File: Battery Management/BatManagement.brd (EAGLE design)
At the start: 87.1 x 71.1 mm, 19 parts, among them J1 RASPBERRYPI-40-PIN-GPIO_PTH, SW1 100SP1T2B4M6QE, X1 87758-1416, X2 87758-1416, X3 22-23-2031, X4 22-23-2031

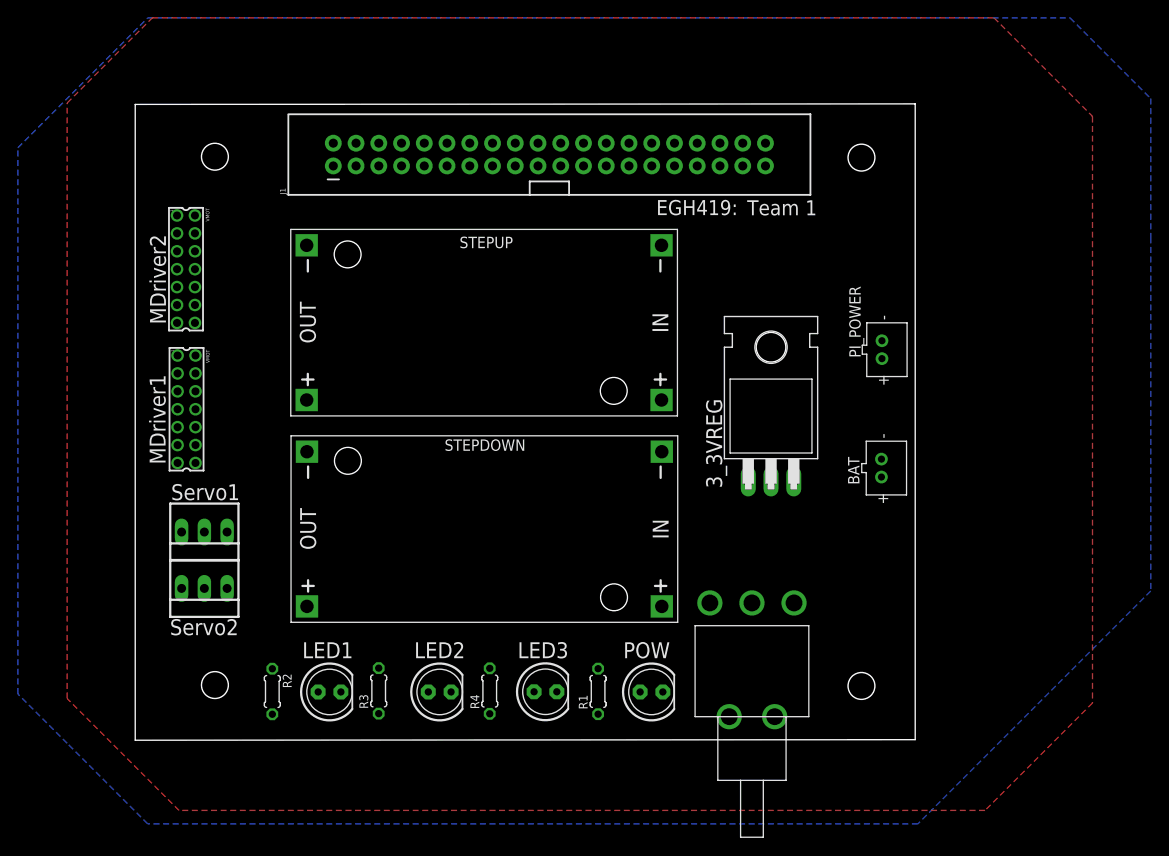
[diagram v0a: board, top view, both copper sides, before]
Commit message: Added jumper for 6V motors
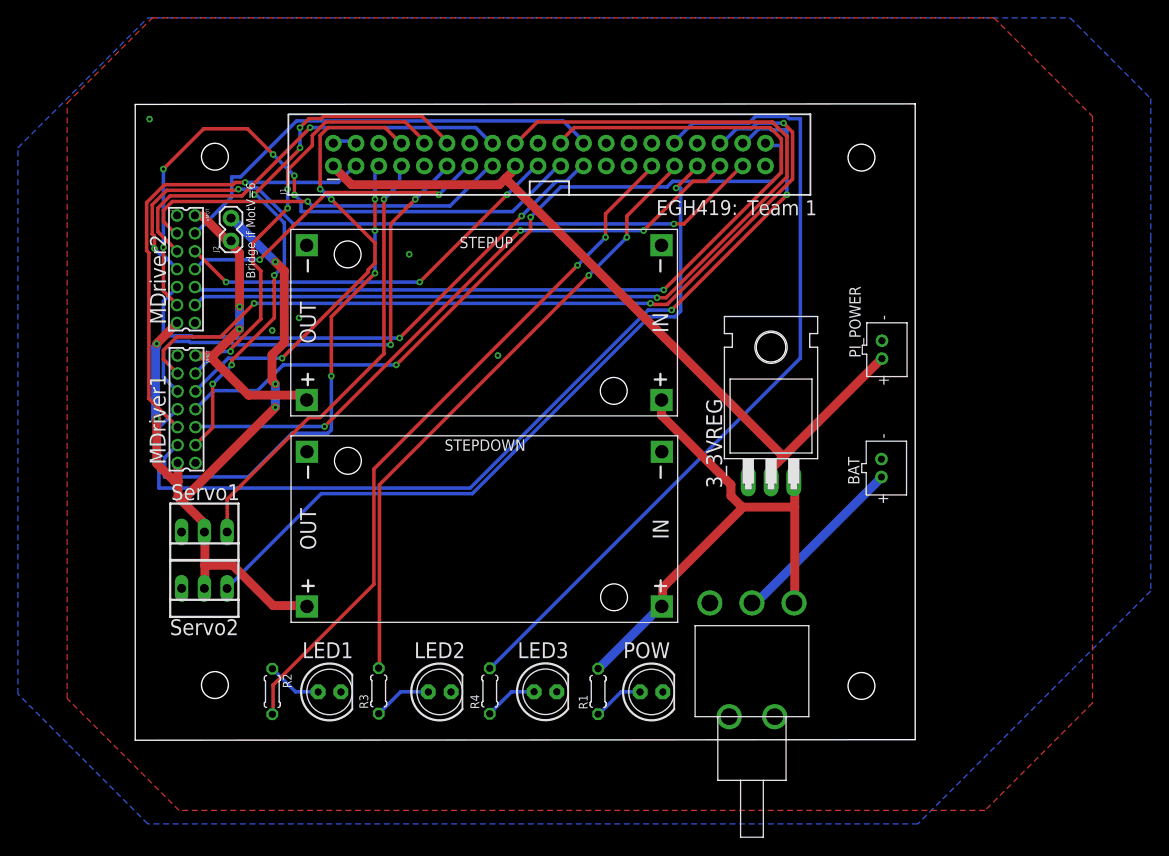
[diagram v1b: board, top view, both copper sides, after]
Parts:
- added J2: (no value), SparkFun-Connectors:1X02
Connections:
- net 5V: now also J2.2
- net ENC1A_1: now also J1.3
- net ENC1A_2: now also J1.23
- net ENC1B_1: now also J1.5
- net ENC1B_2: now also J1.21
- net ENC2A_1: now also J1.8
- net ENC2A_2: now also J1.19
- net ENC2B_1: now also J1.10
- net ENC2B_2: now also J1.24
- net IN3_1: no longer X2.12
- net IN3_2: now also X2.12
- net VMOT: now also J2.1
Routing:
- net IN3_2: track 0.00 -> 108.6 mm, vias 0 -> 1
- net ENA_1: track 0.00 -> 106.3 mm, vias 0 -> 2
- net IN4_2: track 0.00 -> 100.9 mm, vias 0 -> 1
- net IN1_1: track 0.00 -> 96.2 mm, vias 0 -> 3
- net LED3: track 0.00 -> 91.3 mm
- net 5V: track 0.00 -> 87.7 mm, vias 0 -> 5
- net 3_3V: track 0.00 -> 85.2 mm
- net ENB_1: track 0.00 -> 82.1 mm, vias 0 -> 2
- net SERVO2: track 0.00 -> 81.2 mm, vias 0 -> 1
- net ENA_2: track 0.00 -> 79.5 mm, vias 0 -> 3
- net LED1: track 0.00 -> 78.9 mm, vias 0 -> 2
- net IN4_1: track 0.00 -> 70.9 mm, vias 0 -> 3
- net ENC1B_2: track 0.00 -> 69.9 mm, vias 0 -> 5
- net LED2: track 0.00 -> 69.7 mm, vias 0 -> 2
- net IN3_1: track 0.00 -> 61.6 mm, vias 0 -> 6
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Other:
- board text added: "Bridge if MotV=6"

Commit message: Changed to standard header for mdriver connection
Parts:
- removed X1, X2: 87758-1416, con-molex:87758-1416
- added SV1, SV2: (no value), con-lsta:FE07-2
- moved J2 12.8 mm to (23.4, 95.1), turned to 270 degrees
- moved X4 4.85 mm to (26.2, 47.5), turned to 270 degrees
- moved X3 3.28 mm to (30.6, 47.5), turned to 270 degrees
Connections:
- net 5V: now also SV1.1, SV2.1; no longer X1.13, X2.13
- net ENA_1: now also SV1.7; no longer X1.7
- net ENA_2: now also SV2.7; no longer X2.7
- net ENB_1: now also SV1.8; no longer X1.8
- net ENB_2: now also SV2.8; no longer X2.8
- net ENC1A_1: now also SV1.5; no longer X1.9
- net ENC1A_2: now also SV2.5; no longer X2.9
- net ENC1B_1: now also SV1.3; no longer X1.11
- net ENC1B_2: now also SV2.3; no longer X2.11
- net ENC2A_1: now also SV1.10; no longer X1.6
- net ENC2A_2: now also SV2.10; no longer X2.6
- net ENC2B_1: now also SV1.12; no longer X1.4
- net ENC2B_2: now also SV2.12; no longer X2.4
- net GND: now also SV1.13, SV1.2, SV2.13, SV2.2; no longer X1.1, X1.14, X2.1, X2.14
- net IN1_1: now also SV1.11; no longer X1.3
- net IN1_2: now also SV2.11; no longer X2.3
- net IN2_1: now also SV1.9; no longer X1.5
- net IN2_2: now also SV2.9; no longer X2.5
- net IN3_1: now also SV1.4; no longer X1.12
- net IN3_2: now also SV2.4; no longer X2.12
- net IN4_1: now also SV1.6; no longer X1.10
- net IN4_2: now also SV2.6; no longer X2.10
- net VMOT: now also SV1.14, SV2.14; no longer X1.2, X2.2
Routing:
- net ENC2B_2: track 51.1 -> 113.8 mm, vias 0 -> 3
- net IN3_2: track 108.6 -> 54.1 mm
- net IN4_2: track 100.9 -> 57.4 mm, vias 1 -> 0
- net IN3_1: track 61.6 -> 89.1 mm, vias 6 -> 3
- net 5V: track 87.7 -> 65.6 mm, vias 5 -> 0
- net ENC1B_2: track 69.9 -> 51.7 mm, vias 5 -> 4
- net ENA_1: track 106.3 -> 91.9 mm
- net IN4_1: track 70.9 -> 81.2 mm, vias 3 -> 2
- net ENC1B_1: track 56.8 -> 47.1 mm, vias 4 -> 3
- net SERVO2: track 81.2 -> 72.0 mm
- net ENC1A_2: track 61.1 -> 53.0 mm, vias 2 -> 4
- net VMOT: track 34.4 -> 41.6 mm, vias 2 -> 0
- net ENA_2: track 79.5 -> 72.4 mm, vias 3 -> 5
- net IN2_1: track 53.8 -> 47.2 mm, vias 2 -> 3
- net ENC1A_1: track 51.6 -> 45.2 mm, vias 1 -> 3
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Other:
- board text added: "-ve"
- board text added: "Bridge if VMOT=6"
- board text removed: "Bridge if MotV=6"
